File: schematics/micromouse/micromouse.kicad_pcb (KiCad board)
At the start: 2 copper layers, 70 x 90 mm, 36 parts, among them J1 TOF_LEFT, J10 MotorB_Conn, J11 BMI_ConnB, J12 BMI_ConnA, J13 StepDown_{In+}, J14 StepDown_{In-}, J15 StepDown_{Out+}, J16 StepDown_{Out-}, J2 TOF_FRONTLEFT, J3 TOF_FRONTRIGHT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

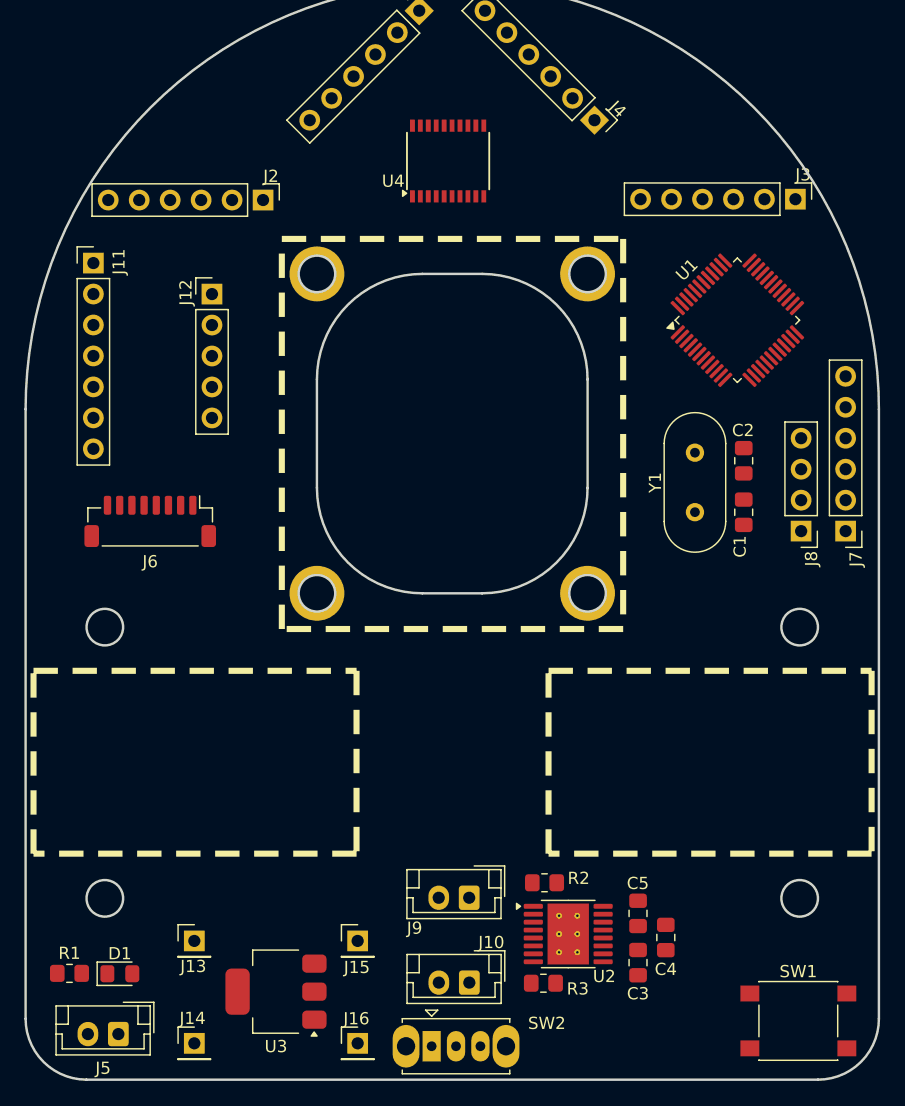
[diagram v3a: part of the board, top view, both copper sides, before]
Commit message: Schematic organized in boxes
Schematic status update:
* STM32 with external clock, DebugPort(*) and communication lines (SPI1, I2C0 and I2C1 and USART1, with pull-up resistors in I2C and USART RX lines) and power lines (VDDs and VSSs)
* First version of power supply schematic [TODO: Check possible short circuit]
* Motor controller schematic
* Mouse sensor connector + mounting holes
* Bluetooth connector for HC-05/HC-06
* TOF schematic using GPIO expander
* BMI160 Mounting holes
* DIP Switches
* Reset and Boot circuits
* LEDs for all voltages lines
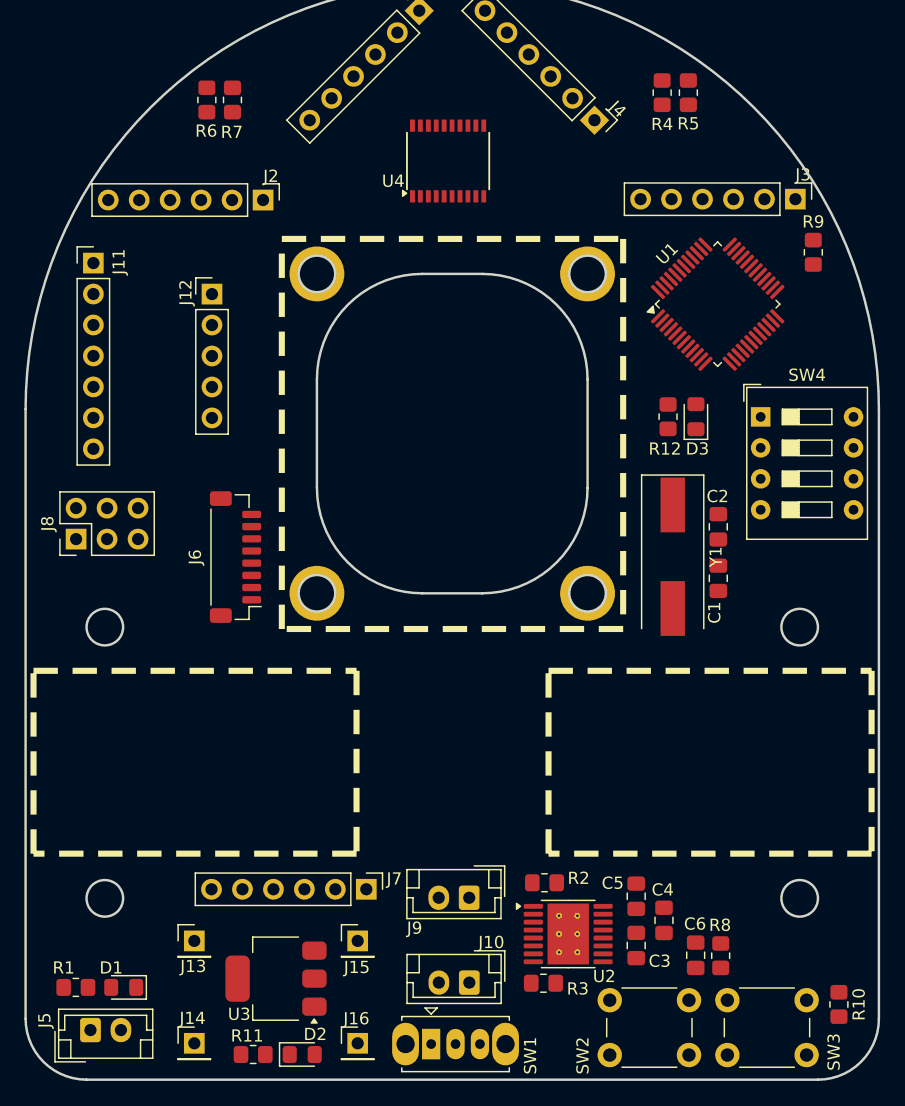
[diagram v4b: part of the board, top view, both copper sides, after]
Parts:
- added C6: 100nF, Capacitor_SMD:C_0805_2012Metric_Pad1.18x1.45mm_HandSolder, F.Cu at (158.3, 101.7)
- added D2: LED, LED_SMD:LED_0805_2012Metric_Pad1.15x1.40mm_HandSolder, F.Cu at (126.1, 109.9)
- added D3: LED, LED_SMD:LED_0805_2012Metric_Pad1.15x1.40mm_HandSolder, F.Cu at (158.4, 57.5)
- added R10: 10k, Resistor_SMD:R_0805_2012Metric_Pad1.20x1.40mm_HandSolder, F.Cu at (170.1, 105.8)
- added R11: 4.7k, Resistor_SMD:R_0805_2012Metric_Pad1.20x1.40mm_HandSolder, F.Cu at (122.0, 109.9)
- added R12: 4.7k, Resistor_SMD:R_0805_2012Metric_Pad1.20x1.40mm_HandSolder, F.Cu at (156.1, 57.5)
- added R4: 2.2k, Resistor_SMD:R_0805_2012Metric_Pad1.20x1.40mm_HandSolder, F.Cu at (155.6, 30.9)
- added R5: 2.2k, Resistor_SMD:R_0805_2012Metric_Pad1.20x1.40mm_HandSolder, F.Cu at (157.8, 30.9)
- added R6: 2.2k, Resistor_SMD:R_0805_2012Metric_Pad1.20x1.40mm_HandSolder, F.Cu at (118.2, 31.6)
- added R7: 2.2k, Resistor_SMD:R_0805_2012Metric_Pad1.20x1.40mm_HandSolder, F.Cu at (120.3, 31.6)
- added R8: 10k, Resistor_SMD:R_0805_2012Metric_Pad1.20x1.40mm_HandSolder, F.Cu at (160.4, 101.8)
- added R9: 10k, Resistor_SMD:R_0805_2012Metric_Pad1.20x1.40mm_HandSolder, F.Cu at (168.0, 44.0)
- added SW3: PB_BOOT, Button_Switch_THT:SW_PUSH_6mm_H5mm, F.Cu at (160.9, 105.4)
- added SW4: SW_DIP_x04, Button_Switch_THT:SW_DIP_SPSTx04_Slide_9.78x12.34mm_W7.62mm_P2.54mm, F.Cu at (163.7, 57.5)
- C1, C2: value C -> 22pF
- J8: footprint Connector_PinHeader_2.54mm:PinHeader_1x04_P2.54mm_Vertical -> Connector_PinHeader_2.54mm:PinHeader_2x03_P2.54mm_Vertical
- R1: value R -> 4.7k
- SW1: value SW_Push -> SW_SPDT; footprint Button_Switch_SMD:SW_SPST_PTS645 -> Button_Switch_THT:SW_Slide_SPDT_Straight_CK_OS102011MS2Q
- SW2: value SW_SPDT -> PB_RESET; footprint Button_Switch_THT:SW_Slide_SPDT_Straight_CK_OS102011MS2Q -> Button_Switch_THT:SW_PUSH_6mm_H5mm
- Y1: footprint Crystal:Crystal_HC49-4H_Vertical -> Crystal:Crystal_SMD_HC49-SD
- moved J8 59.5 mm to (107.5, 67.6), turned to 90 degrees
- moved J7 49.1 mm to (131.3, 96.3), turned to -90 degrees
- moved SW1 30.2 mm to (136.7, 109.0)
- moved SW2 15.1 mm to (151.3, 105.4)
- moved Y1 8.73 mm to (156.5, 69.0)
- moved J6 7.59 mm to (120.6, 69.0), turned to 90 degrees
- moved C1 5.81 mm to (160.2, 70.8)
- moved C2 5.81 mm to (160.2, 66.6)
- moved J5 2.31 mm to (108.7, 107.8), turned to 0 degrees
- moved U1 2.09 mm to (160.2, 48.3)
- moved C3 1.42 mm to (153.5, 100.9)
- moved C4 1.42 mm to (155.8, 98.8)
- moved C5 1.42 mm to (153.5, 96.9)
- moved R1 1.26 mm to (107.5, 104.3), turned to 180 degrees
- moved D1 1.16 mm to (111.4, 104.3), turned to 180 degrees
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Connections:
- D1 pad 1: VCC_{3.3} -> Net-(D1-K)
- D1 pad 2: Net-(D1-A) -> VCC_{7.4}
- J8 pad 1: unconnected-(J8-Pin_1-Pad1) -> /RESET
- J8 pad 2: unconnected-(J8-Pin_2-Pad2) -> VCC_{3.3}
- J8 pad 3: unconnected-(J8-Pin_3-Pad3) -> /SW_{clk}
- J8 pad 4: unconnected-(J8-Pin_4-Pad4) -> /SW_{dio}
- R1 pad 1: GND -> Net-(D1-K)
- R1 pad 2: VCC_{3.3} -> GND
- SW1 pad 1: unconnected-(SW1-Pad1) -> Net-(SW1-A)
- SW1 pad 2: unconnected-(SW1-Pad2) -> VCC_{5}
- SW2 pad 1: Net-(SW2-A) -> GND
- SW2 pad 2: VCC_{5} -> /RESET
- U1 pad 1: unconnected-(U1-VBAT-Pad1) -> VCC_{3.3}
- U1 pad 23: Net-(U1-VSS-Pad23) -> GND
- U1 pad 24: unconnected-(U1-VDD-Pad24) -> VCC_{3.3}
- U1 pad 35: Net-(U1-VSS-Pad23) -> GND
- U1 pad 36: unconnected-(U1-VDD-Pad36) -> VCC_{3.3}
- U1 pad 39: unconnected-(U1-PB3-Pad39) -> /PB3
- U1 pad 44: unconnected-(U1-BOOT0-Pad44) -> /BOOT
- U1 pad 47: Net-(U1-VSS-Pad23) -> GND
- U1 pad 48: unconnected-(U1-VDD-Pad48) -> VCC_{3.3}
- U1 pad 7: unconnected-(U1-NRST-Pad7) -> /RESET
- U1 pad 8: unconnected-(U1-VSSA-Pad8) -> GND
- U1 pad 9: unconnected-(U1-VDDA-Pad9) -> VCC_{3.3}
- U3 pad 2: Net-(D1-A) -> VCC_{3.3}
- U3 pad 3: Net-(SW2-A) -> Net-(SW1-A)

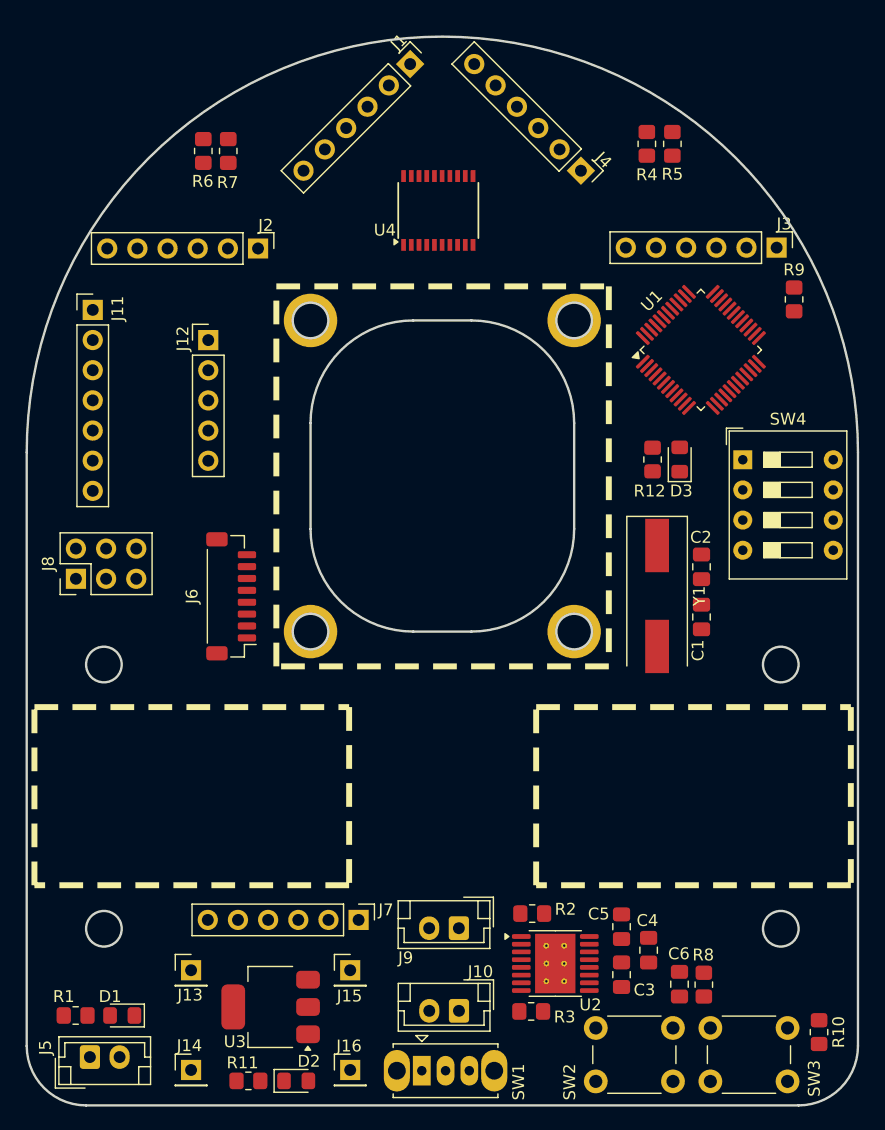
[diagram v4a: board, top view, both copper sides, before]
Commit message: Schematic status: * STM32 with external clock, DebugPort(*) and communication lines (SPI1, I2C1 and I2C2 and USART1, with pull-up resistors in I2C and USART RX lines) and power lines (VDDs and VSSs) * Motor driver with encoders connections * Programming header * Bluetooth/USART connector * Power LED indicators * Power supply * Reset and boot mode buttons * Mouse sensor with mounting holes * Flash memory (SPI nor flash) * Accelerometer+Gyro mounting holes * Distance sensors (GPIO expander + TOF connectors) * User LEDs and switches (GPIO expander + 4x LEDs + 4x switches)
PCB:
* Reorganized pcb board to use space below motors

ToDo:
* Connect signals to the microcontroller in the schematic (signals are listed in priority order at the top)
* Create tracks and planes in the PCB
* Validate the design
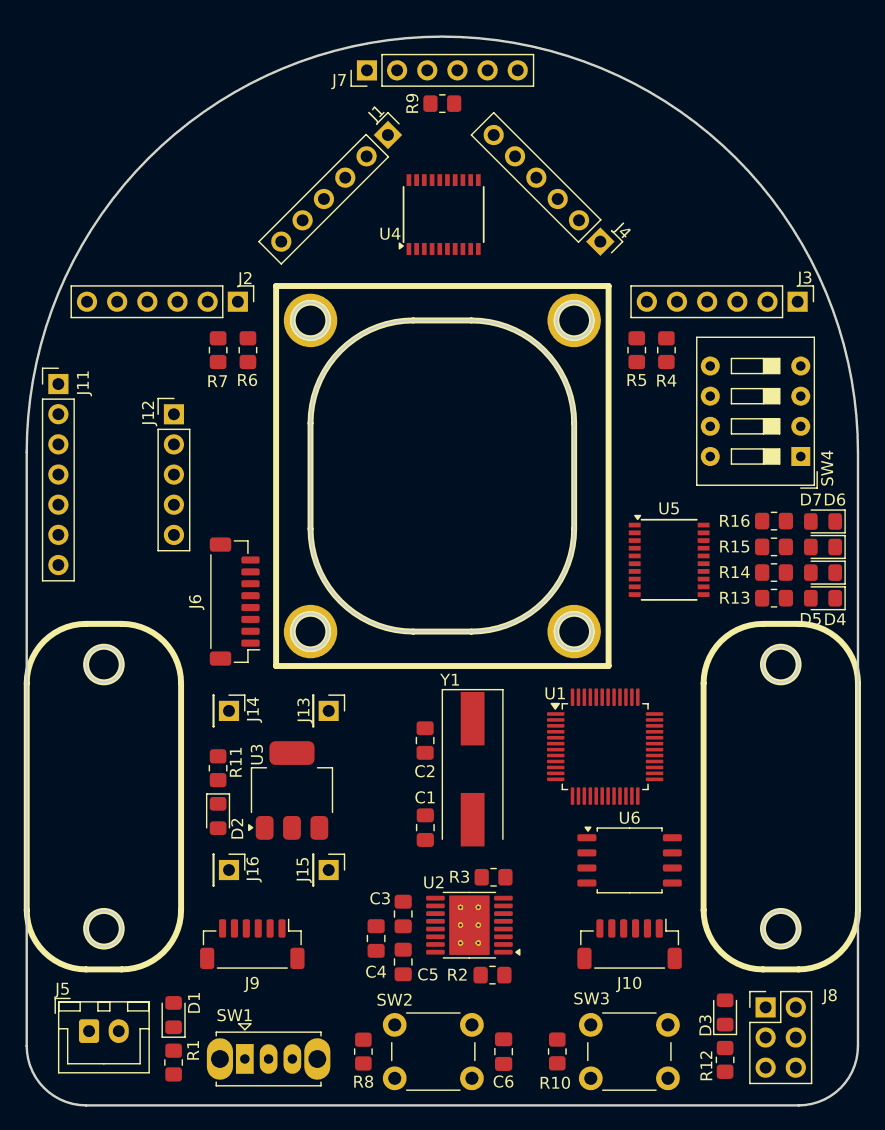
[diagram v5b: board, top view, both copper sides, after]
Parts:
- added D4: LED, LED_SMD:LED_0805_2012Metric_Pad1.15x1.40mm_HandSolder, F.Cu at (170.4, 69.2)
- added D5: LED, LED_SMD:LED_0805_2012Metric_Pad1.15x1.40mm_HandSolder, F.Cu at (170.4, 67.1)
- added D6: LED, LED_SMD:LED_0805_2012Metric_Pad1.15x1.40mm_HandSolder, F.Cu at (170.4, 64.9)
- added D7: LED, LED_SMD:LED_0805_2012Metric_Pad1.15x1.40mm_HandSolder, F.Cu at (170.4, 62.7)
- added R13: 4.7k, Resistor_SMD:R_0805_2012Metric_Pad1.20x1.40mm_HandSolder, F.Cu at (166.3, 69.2)
- added R14: 4.7k, Resistor_SMD:R_0805_2012Metric_Pad1.20x1.40mm_HandSolder, F.Cu at (166.3, 67.0)
- added R15: 4.7k, Resistor_SMD:R_0805_2012Metric_Pad1.20x1.40mm_HandSolder, F.Cu at (166.3, 64.9)
- added R16: 4.7k, Resistor_SMD:R_0805_2012Metric_Pad1.20x1.40mm_HandSolder, F.Cu at (166.3, 62.7)
- added U5: PCF8574TS, Package_SO:SSOP-20_4.4x6.5mm_P0.65mm, F.Cu at (157.5, 66.0)
- added U6: W25Q32JVSS, Package_SO:SOIC-8_5.23x5.23mm_P1.27mm, F.Cu at (154.2, 91.3)
- J10, J9: footprint Connector_JST:JST_EH_B2B-EH-A_1x02_P2.50mm_Vertical -> Connector_JST:JST_SH_BM06B-SRSS-TB_1x06-1MP_P1.00mm_Vertical
- J5: footprint Connector_JST:JST_EH_B2B-EH-A_1x02_P2.50mm_Vertical -> Connector_JST:JST_XH_B2B-XH-A_1x02_P2.50mm_Vertical
- moved J7 71.5 mm to (132.0, 24.8), turned to 90 degrees
- moved J8 68.4 mm to (165.6, 103.7), turned to 0 degrees
- moved R12 50.9 mm to (162.2, 108.1)
- moved D3 46.7 mm to (162.2, 104.1)
- moved U1 34.4 mm to (152.1, 81.7), turned to 0 degrees
- moved R9 33.9 mm to (138.4, 27.6), turned to 180 degrees
- moved J14 30.4 mm to (120.4, 78.7), turned to -90 degrees
- moved C1 29.2 mm to (136.9, 88.5)
- moved R8 29.2 mm to (131.7, 107.4), turned to -90 degrees
- moved C2 27.5 mm to (136.9, 81.2)
- moved R11 26.5 mm to (119.5, 83.5), turned to 90 degrees
- moved J13 24.7 mm to (128.8, 78.7), turned to -90 degrees
- moved D2 23.3 mm to (119.5, 87.6), turned to -90 degrees
- moved C4 23.0 mm to (132.8, 97.9), turned to -90 degrees
- moved R10 22.1 mm to (148.1, 107.4), turned to 90 degrees
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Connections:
- J10 pad 2: Net-(J10-Pin_2) -> GND
- J13 pad 1: VCC_{7.4} -> GND
- J14 pad 1: GND -> VCC_{7.4}
- J15 pad 1: VCC_{5} -> GND
- J16 pad 1: GND -> VCC_{5}
- J9 pad 2: Net-(J9-Pin_2) -> GND
- SW1 pad 3: GND -> unconnected-(SW1-C-Pad3)
- SW4 pad 1: VCC_{3.3} -> Net-(U5-P4)
- SW4 pad 2: VCC_{3.3} -> Net-(U5-P5)
- SW4 pad 3: VCC_{3.3} -> Net-(U5-P6)
- SW4 pad 4: VCC_{3.3} -> Net-(U5-P7)
- SW4 pad 5: /SW4 -> VCC_{3.3}
- SW4 pad 6: /SW3 -> VCC_{3.3}
- SW4 pad 7: /SW2 -> VCC_{3.3}
- SW4 pad 8: /SW1 -> VCC_{3.3}
- U2 pad 4: Net-(J9-Pin_2) -> Net-(J9-Pin_6)
- U2 pad 5: Net-(J10-Pin_2) -> Net-(J10-Pin_6)

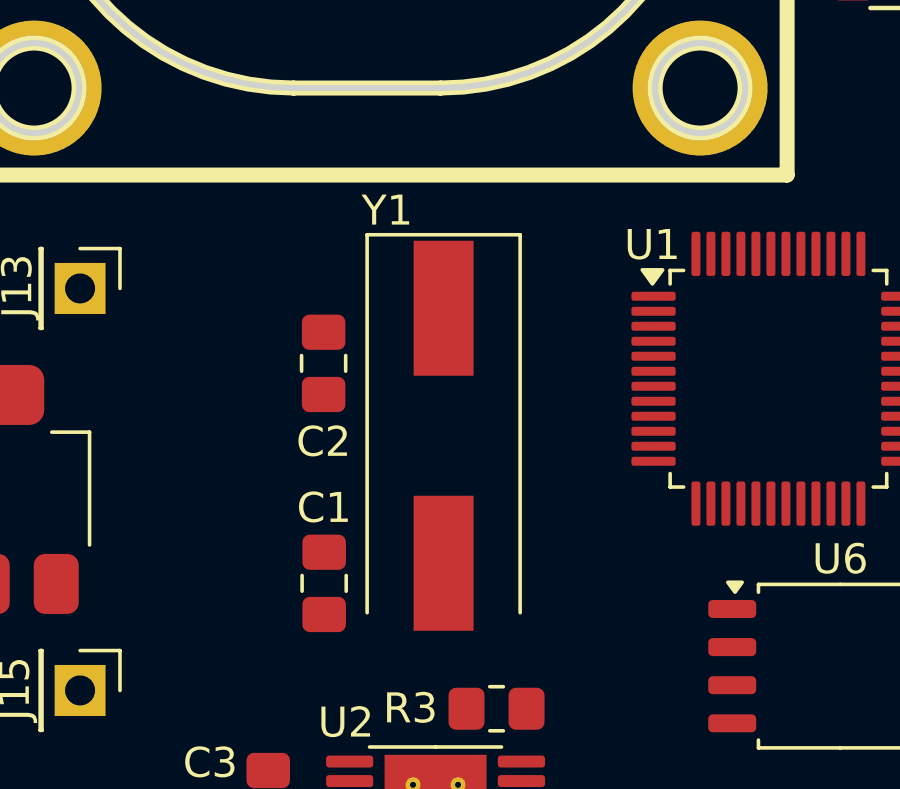
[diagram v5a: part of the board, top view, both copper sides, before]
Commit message: Add second Crystal for second footprint with holes
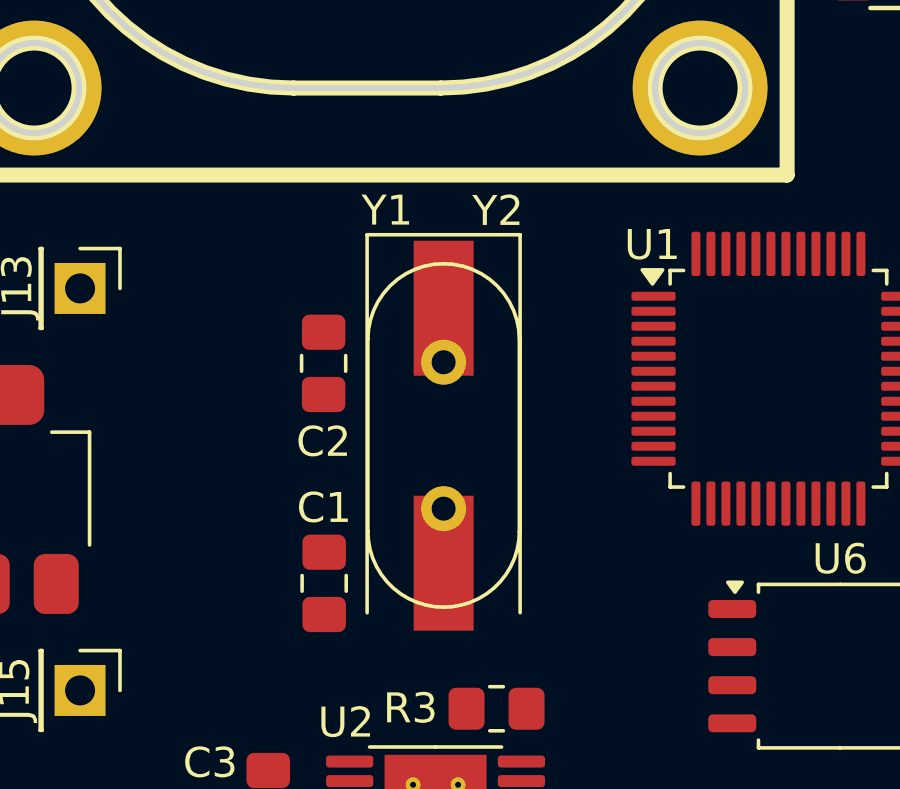
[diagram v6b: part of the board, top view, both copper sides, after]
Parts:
- added Y2: Crystal (8MHz), Crystal:Crystal_HC49-4H_Vertical, F.Cu at (140.9, 81.2)
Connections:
- J12 pad 2: /BMI_{int2} -> unconnected-(J12-Pin_2-Pad2)
- J12 pad 4: unconnected-(J12-Pin_4-Pad4) -> /BMI_{int2}
- J7 pad 2: /USART_{RX} -> /USART1_{RX}
- J7 pad 3: /USART_{TX} -> /USART1_{TX}
- U5 pad 1: /TOF_{int} -> unconnected-(U5-~{INT}-Pad1)
